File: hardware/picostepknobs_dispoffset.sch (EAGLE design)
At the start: 56 parts, among them J1 AUDIO-JACK-TRRS, J2 AUDIO-JACK-TRRS, P1 10k, P2 10k, P3 10k, P4 10k, P5 10k, P6 10k, P7 10k, P8 10k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

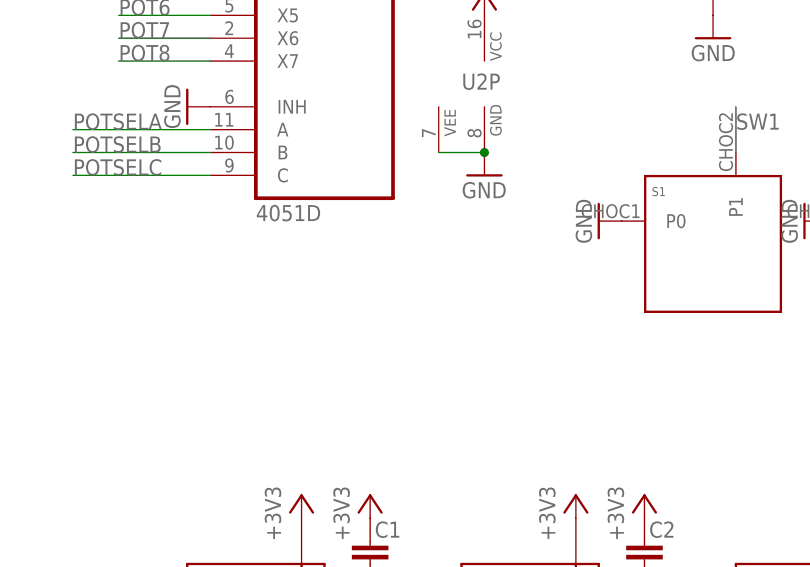
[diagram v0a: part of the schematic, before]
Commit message: oops forgot bypass cap on 4051
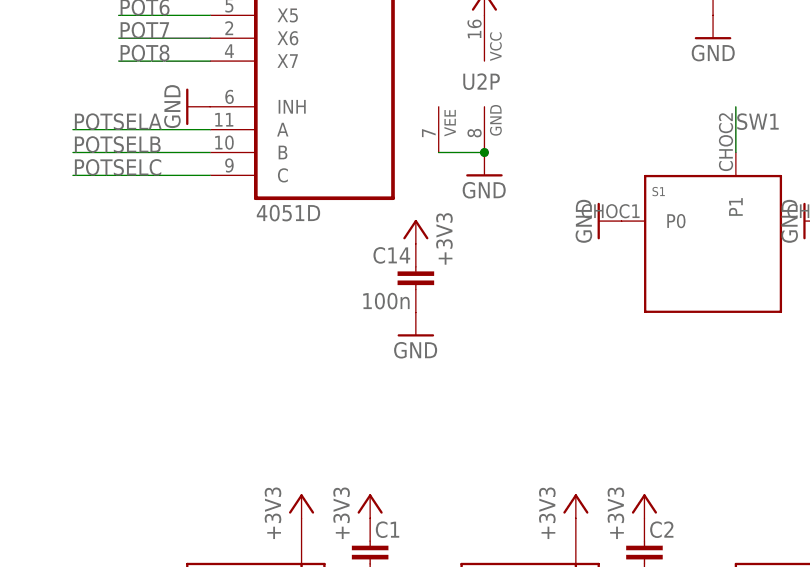
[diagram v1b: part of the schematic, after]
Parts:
- added C14: 100n, rcl:C-EUC0805
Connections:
- net +3V3: now also C14.1
- net GND: now also C14.2
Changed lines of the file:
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@@
 <part name="U1" library="RpiPico" deviceset="RASPBERRY_PICO" device="SMD-TH"/>
 <part name="MODULE_DISP1" library="todstuff2023" deviceset="DISPLAY-OLED-128X64" device="-1.3IN"/>
+<part name="C14" library="rcl" library_urn="urn:adsk.eagle:library:334" deviceset="C-EU" device="C0805" package3d_urn="urn:adsk.eagle:package:23617/2" value="100n"/>
+<part name="GND49" library="supply1" library_urn="urn:adsk.eagle:library:371" deviceset="GND" device=""/>
+<part name="+3V38" library="supply1" library_urn="urn:adsk.eagle:library:371" deviceset="+3V3" device=""/>
 </parts>
 <sheets>
@@
 <attribute name="VALUE" x="48.26" y="106.68" size="1.778" layer="96"/>
 </instance>
+<instance part="C14" gate="G$1" x="127" y="187.96" smashed="yes" rot="MR0">
+<attribute name="NAME" x="126.492" y="188.341" size="1.778" layer="95" rot="MR0"/>
+<attribute name="VALUE" x="126.492" y="183.261" size="1.778" layer="96" rot="MR0"/>
+</instance>
+<instance part="GND49" gate="1" x="127" y="180.34" smashed="yes">
+<attribute name="VALUE" x="124.46" y="177.8" size="1.778" layer="96"/>
+</instance>
+<instance part="+3V38" gate="G$1" x="127" y="193.04" smashed="yes">
+<attribute name="VALUE" x="131.064" y="187.96" size="1.778" layer="96" rot="R90"/>
+</instance>
 </instances>
 <busses>
@@
 <pinref part="C12" gate="G$1" pin="2"/>
 <pinref part="GND48" gate="1" pin="GND"/>
+</segment>
+<segment>
+<pinref part="C14" gate="G$1" pin="2"/>
+<pinref part="GND49" gate="1" pin="GND"/>
 </segment>
 </net>
@@
 <pinref part="+3V37" gate="G$1" pin="+3V3"/>
 </segment>
+<segment>
+<pinref part="C14" gate="G$1" pin="1"/>
+<pinref part="+3V38" gate="G$1" pin="+3V3"/>
+</segment>
 </net>

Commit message: it is working a little
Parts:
- LED1, LED10, LED11, LED12, LED2, LED3, LED4, LED5, LED6, LED7, LED8, LED9: value WS2812B3535 -> WS2812B5050; device todstuff2023:WS2812B3535 -> todstuff2023:WS2812B5050
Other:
- moved on the sheet: C14, U2, U2P

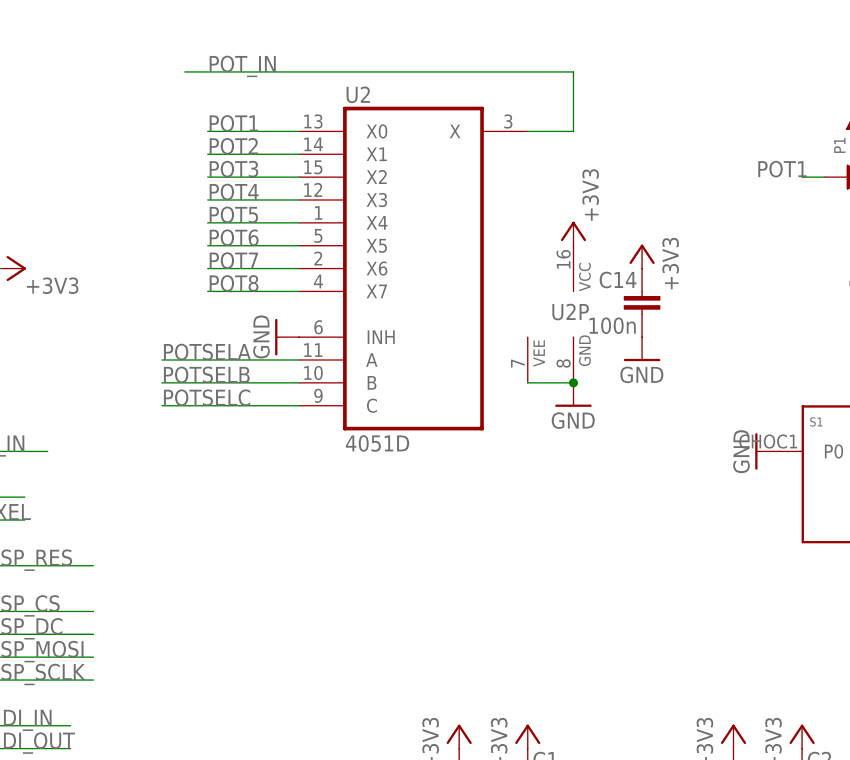
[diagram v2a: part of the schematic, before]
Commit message: keep proto version for posterity
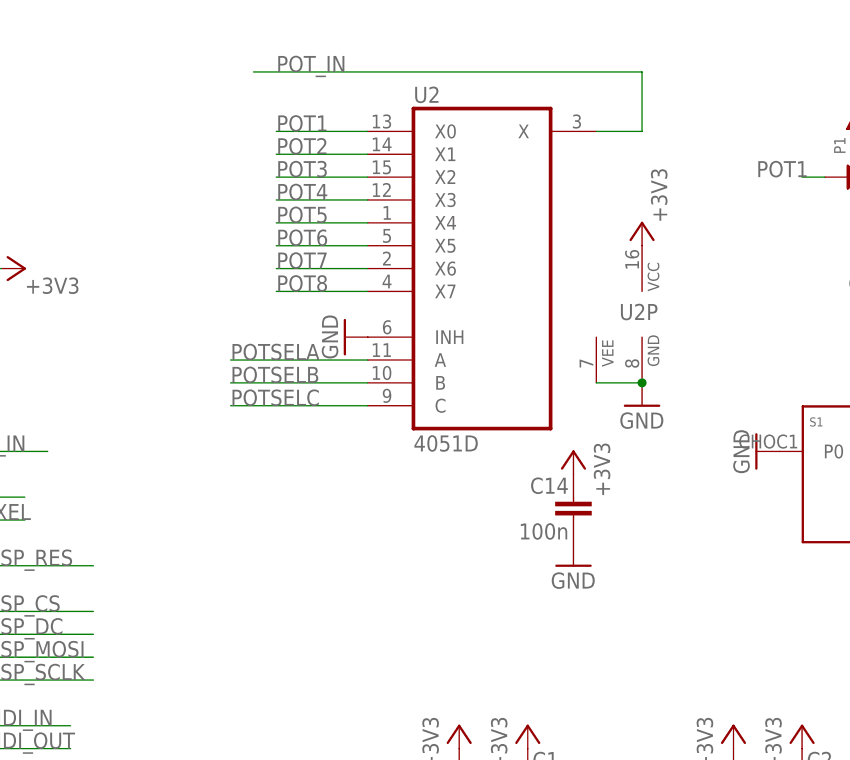
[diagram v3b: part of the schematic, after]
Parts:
- LED1, LED10, LED11, LED12, LED2, LED3, LED4, LED5, LED6, LED7, LED8, LED9: value WS2812B5050 -> WS2812B3535; device todstuff2023:WS2812B5050 -> todstuff2023:WS2812B3535
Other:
- moved on the sheet: C14, U2, U2P
